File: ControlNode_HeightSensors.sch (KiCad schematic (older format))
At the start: 2 parts

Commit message: Update height sensors.
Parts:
- removed P? (x2): CONN_01X05, symbol CONN_01X05
- added C? (x3): C_100nF_50V, RLOOP_FOOTPRINTS:rLoop_C_0603, symbol C_100nF_50V
- added P? (x3): TE_640456-8, RLOOP_FOOTPRINTS:rLoop_TE640456-8, symbol TE_640456-8
- added R? (x3): 2.2K, RLOOP_FOOTPRINTS:rLoop_R_0603, symbol 2.2K
- added U? (x3): DS8921AMX, RLOOP_FOOTPRINTS:rLoop_SOIC8, symbol DS8921AMX
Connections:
- net labels added: +24V_A, +5V_A, GNDD, HEIGHT_FL_RX_3V, HEIGHT_FL_TX, HEIGHT_FR_RX_3V, HEIGHT_FR_TX, HEIGHT_RL_RX_3V, HEIGHT_RL_TX
- net labels removed: +24V, A2, A3, GND
- wire segments 16 -> 57
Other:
- note removed: "Height Sensors 5 Pin"

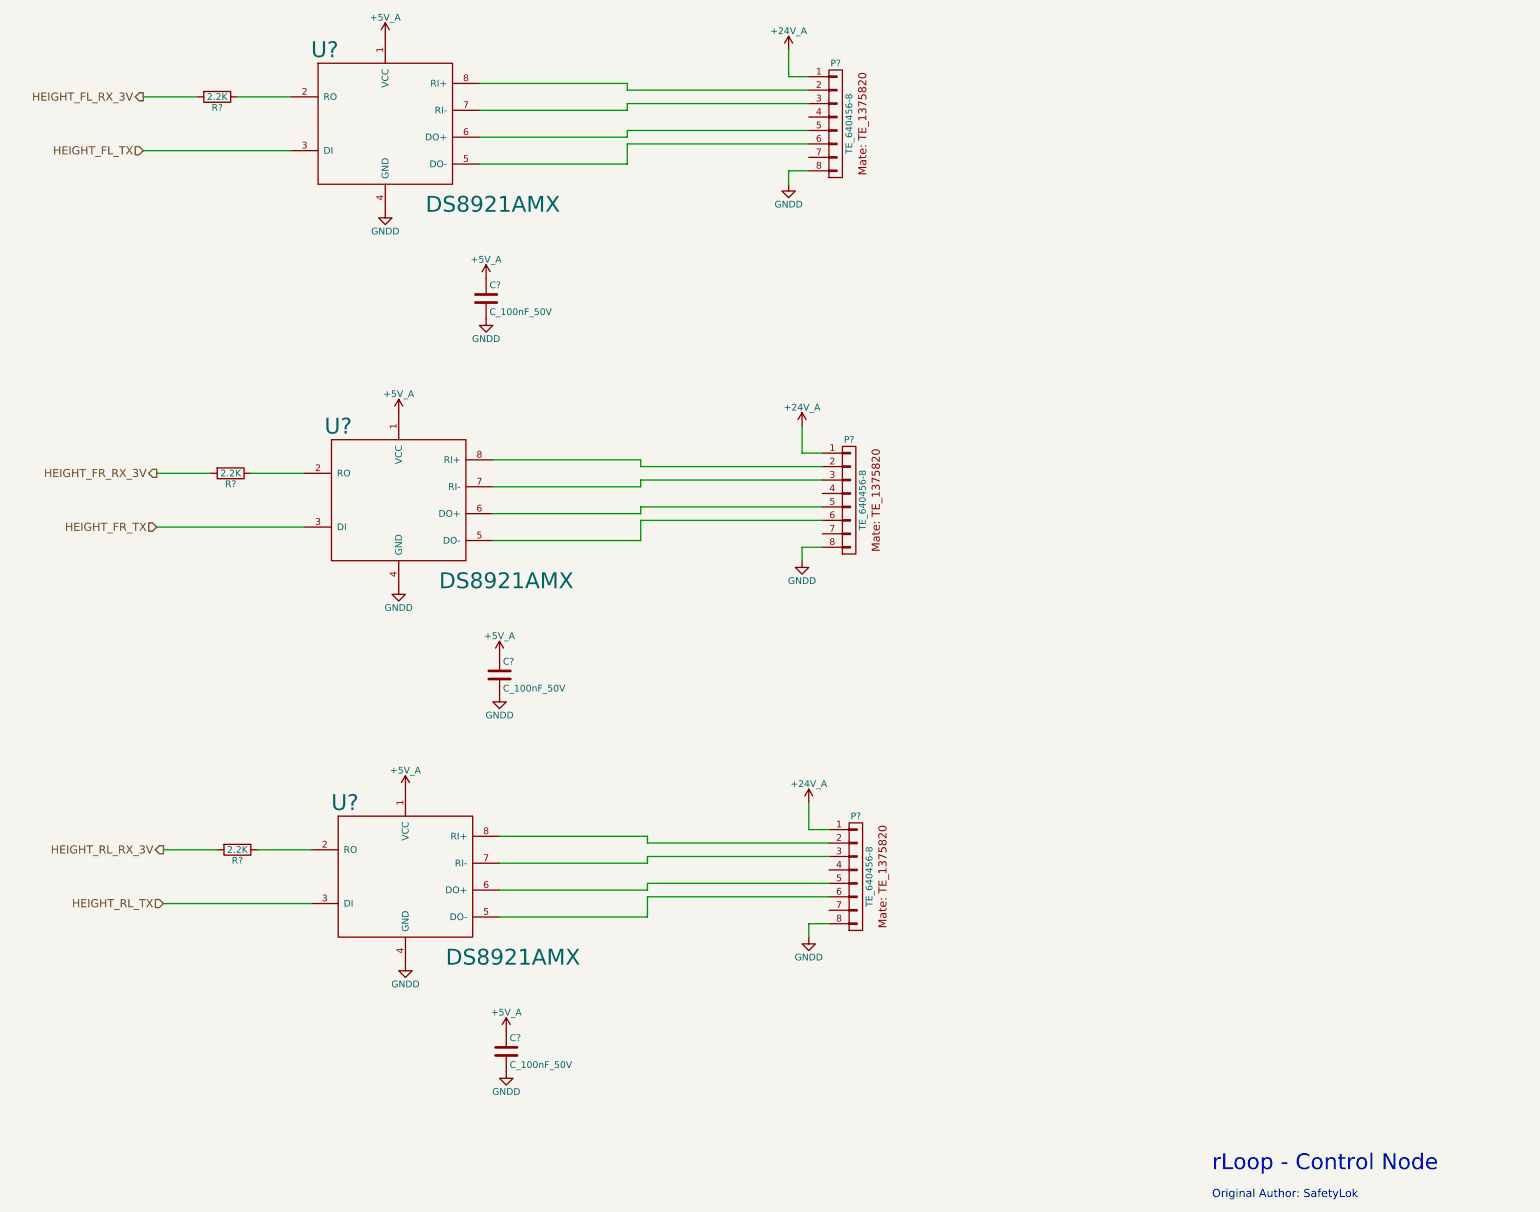
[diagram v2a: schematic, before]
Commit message: Update 10K pullups, 100R on RS422's and additional bypass caps.
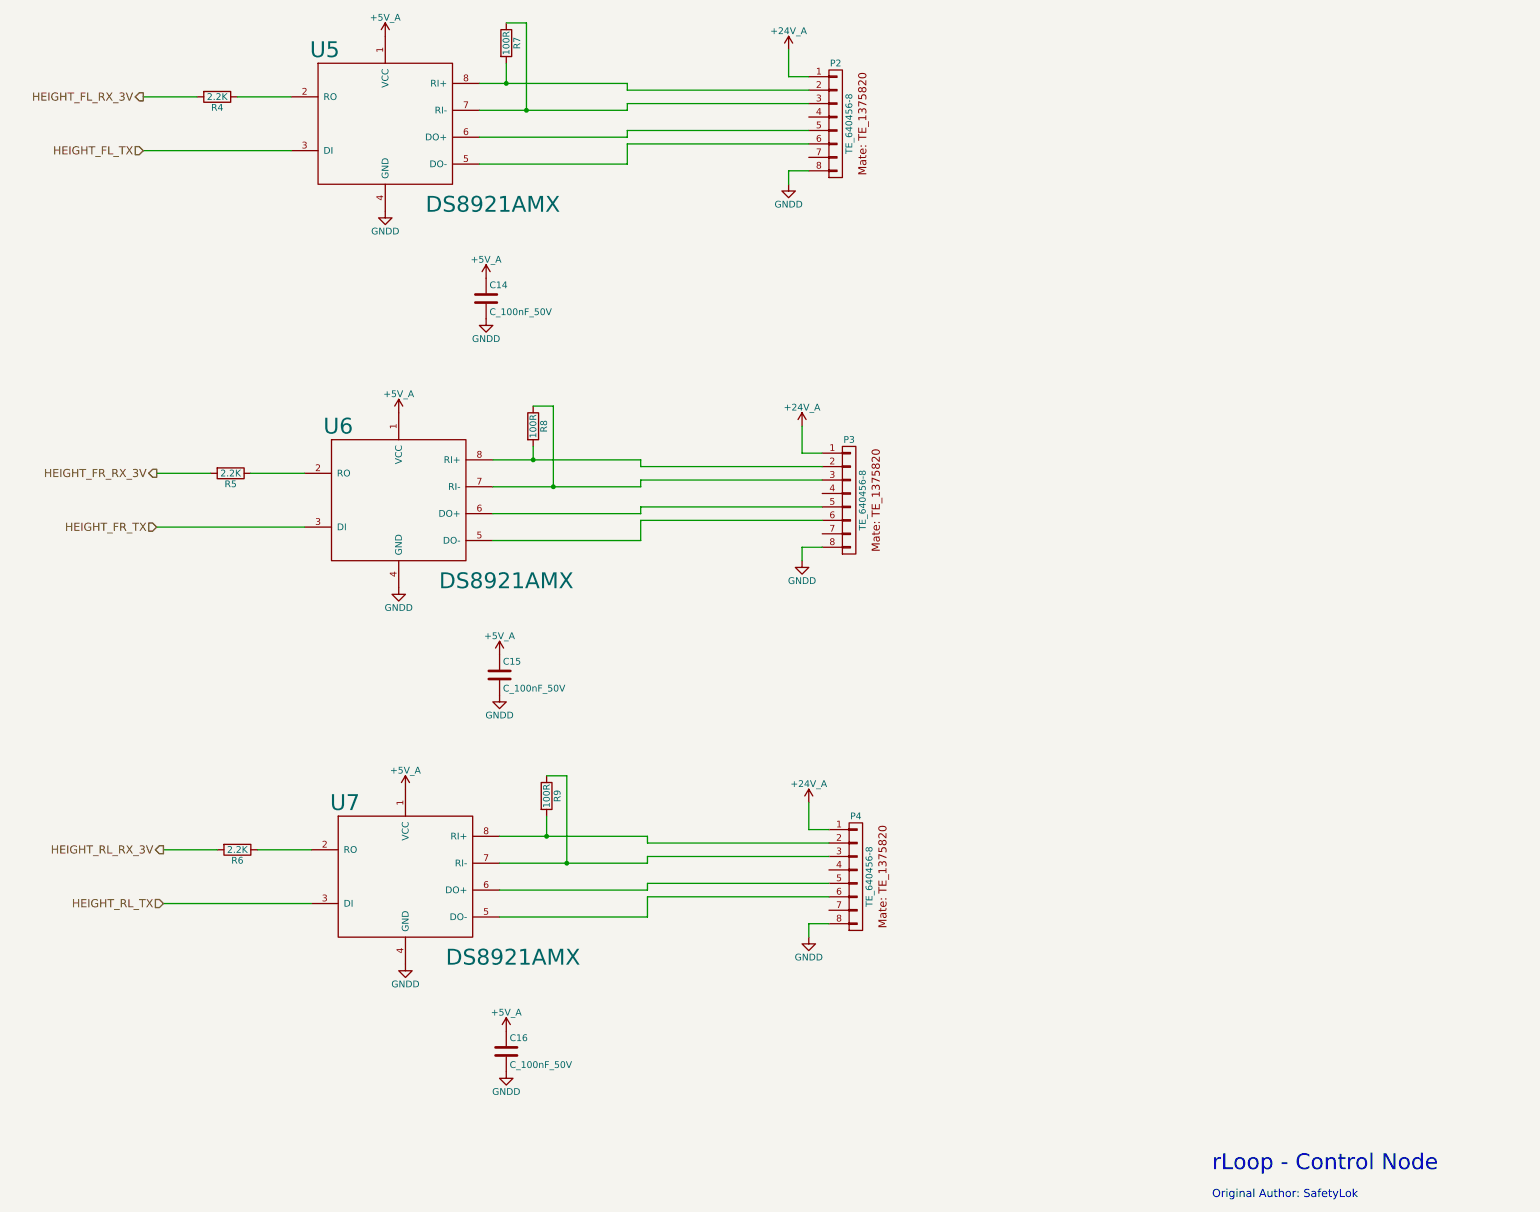
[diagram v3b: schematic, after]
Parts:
- added R7, R8, R9: 100R, RLOOP_FOOTPRINTS:rLoop_R_0603, symbol 100R
- gave numbers to parts that had none: 12
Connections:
- net at P2.2 (P2), U5.8 (RI+): now also R7.2
- net at P2.3 (P3), U5.7 (RI-): now also R7.1
- net at P3.2 (P2), U6.8 (RI+): now also R8.2
- net at P3.3 (P3), U6.7 (RI-): now also R8.1
- net at P4.2 (P2), U7.8 (RI+): now also R9.2
- net at P4.3 (P3), U7.7 (RI-): now also R9.1
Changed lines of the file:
@@
 Original Author: SafetyLok
 $Comp
-L TE_640456-8 P?
+L TE_640456-8 P2
 U 1 1 575BF630
 P 9100 2000
-F 0 "P?" H 9150 2050 50  0000 C CNN
+F 0 "P2" H 9150 2050 50  0000 C CNN
 F 1 "TE_640456-8" V 9250 1600 50  0000 C CNN
 F 2 "RLOOP_FOOTPRINTS:rLoop_TE640456-8" H 9150 1600 50  0001 C CNN
@@
 $EndComp
 $Comp
-L +24V_A #PWR?
+L +24V_A #PWR58
 U 1 1 575BF637
 P 8800 1850
-F 0 "#PWR?" H 8800 1700 50  0001 C CNN
+F 0 "#PWR58" H 8800 1700 50  0001 C CNN
 F 1 "+24V_A" H 8800 1990 50  0000 C CNN
 F 2 "" H 8800 1850 60  0000 C CNN
@@
 $EndComp
 $Comp
-L GNDD #PWR?
+L GNDD #PWR59
 U 1 1 575BF63D
 P 8800 2850
-F 0 "#PWR?" H 8800 2600 50  0001 C CNN
+F 0 "#PWR59" H 8800 2600 50  0001 C CNN
 F 1 "GNDD" H 8800 2700 50  0000 C CNN
 F 2 "" H 8800 2850 50  0000 C CNN
@@
 	8800 2750 8800 2850
 $Comp
-L DS8921AMX U?
+L DS8921AMX U5
 U 1 1 575BF647
 P 5300 1950
-F 0 "U?" H 5350 2050 118 0000 C CNN
+F 0 "U5" H 5350 2050 118 0000 C CNN
 F 1 "DS8921AMX" H 6600 900 118 0000 C CNN
 F 2 "RLOOP_FOOTPRINTS:rLoop_SOIC8" H 5250 1950 118 0001 C CNN
@@
 $EndComp
 $Comp
-L GNDD #PWR?
+L GNDD #PWR47
 U 1 1 575BF64E
 P 5800 3050
-F 0 "#PWR?" H 5800 2800 50  0001 C CNN
+F 0 "#PWR47" H 5800 2800 50  0001 C CNN
 F 1 "GNDD" H 5800 2900 50  0000 C CNN
 F 2 "" H 5800 3050 50  0000 C CNN
@@
 $EndComp
 $Comp
-L C_100nF_50V C?
+L C_100nF_50V C14
 U 1 1 575BF654
 P 6550 3700
-F 0 "C?" H 6575 3800 50  0000 L CNN
+F 0 "C14" H 6575 3800 50  0000 L CNN
 F 1 "C_100nF_50V" H 6575 3600 50  0000 L CNN
 F 2 "RLOOP_FOOTPRINTS:rLoop_C_0603" H 6588 3550 50  0001 C CNN
@@
 $EndComp
 $Comp
-L GNDD #PWR?
+L GNDD #PWR53
 U 1 1 575BF65B
 P 6550 3850
-F 0 "#PWR?" H 6550 3600 50  0001 C CNN
+F 0 "#PWR53" H 6550 3600 50  0001 C CNN
 F 1 "GNDD" H 6550 3700 50  0000 C CNN
 F 2 "" H 6550 3850 50  0000 C CNN
@@
 	7600 2550 8950 2550
 $Comp
-L +5V_A #PWR?
+L +5V_A #PWR46
 U 1 1 575BF66D
 P 5800 1750
-F 0 "#PWR?" H 5800 1600 50  0001 C CNN
+F 0 "#PWR46" H 5800 1600 50  0001 C CNN
 F 1 "+5V_A" H 5800 1890 50  0000 C CNN
 F 2 "" H 5800 1750 60  0000 C CNN
@@
 $EndComp
 $Comp
-L +5V_A #PWR?
+L +5V_A #PWR52
 U 1 1 575BF673
 P 6550 3550
-F 0 "#PWR?" H 6550 3400 50  0001 C CNN
+F 0 "#PWR52" H 6550 3400 50  0001 C CNN
 F 1 "+5V_A" H 6550 3690 50  0000 C CNN
 F 2 "" H 6550 3550 60  0000 C CNN
@@
 $EndComp
 $Comp
-L 2.2K R?
+L 2.2K R4
 U 1 1 575BF679
 P 4550 2200
-F 0 "R?" V 4630 2200 50  0000 C CNN
+F 0 "R4" V 4630 2200 50  0000 C CNN
 F 1 "2.2K" V 4550 2200 50  0000 C CNN
 F 2 "RLOOP_FOOTPRINTS:rLoop_R_0603" V 4480 2200 50  0001 C CNN
@@
 HEIGHT_FL_TX
 $Comp
-L TE_640456-8 P?
+L TE_640456-8 P3
 U 1 1 575BF685
 P 9200 4800
-F 0 "P?" H 9250 4850 50  0000 C CNN
+F 0 "P3" H 9250 4850 50  0000 C CNN
 F 1 "TE_640456-8" V 9350 4400 50  0000 C CNN
 F 2 "RLOOP_FOOTPRINTS:rLoop_TE640456-8" H 9250 4400 50  0001 C CNN
@@
 $EndComp
 $Comp
-L +24V_A #PWR?
+L +24V_A #PWR60
 U 1 1 575BF68C
 P 8900 4650
-F 0 "#PWR?" H 8900 4500 50  0001 C CNN
+F 0 "#PWR60" H 8900 4500 50  0001 C CNN
 F 1 "+24V_A" H 8900 4790 50  0000 C CNN
 F 2 "" H 8900 4650 60  0000 C CNN
@@
 $EndComp
 $Comp
-L GNDD #PWR?
+L GNDD #PWR61
 U 1 1 575BF692
 P 8900 5650
-F 0 "#PWR?" H 8900 5400 50  0001 C CNN
+F 0 "#PWR61" H 8900 5400 50  0001 C CNN
 F 1 "GNDD" H 8900 5500 50  0000 C CNN
 F 2 "" H 8900 5650 50  0000 C CNN
@@
 	8900 5550 8900 5650
 $Comp
-L DS8921AMX U?
+L DS8921AMX U6
 U 1 1 575BF69C
 P 5400 4750
-F 0 "U?" H 5450 4850 118 0000 C CNN
+F 0 "U6" H 5450 4850 118 0000 C CNN
 F 1 "DS8921AMX" H 6700 3700 118 0000 C CNN
 F 2 "RLOOP_FOOTPRINTS:rLoop_SOIC8" H 5350 4750 118 0001 C CNN
@@
 $EndComp
 $Comp
-L GNDD #PWR?
+L GNDD #PWR49
 U 1 1 575BF6A3
 P 5900 5850
-F 0 "#PWR?" H 5900 5600 50  0001 C CNN
+F 0 "#PWR49" H 5900 5600 50  0001 C CNN
 F 1 "GNDD" H 5900 5700 50  0000 C CNN
 F 2 "" H 5900 5850 50  0000 C CNN
@@
 $EndComp
 $Comp
-L C_100nF_50V C?
+L C_100nF_50V C15
 U 1 1 575BF6A9
 P 6650 6500
-F 0 "C?" H 6675 6600 50  0000 L CNN
+F 0 "C15" H 6675 6600 50  0000 L CNN
 F 1 "C_100nF_50V" H 6675 6400 50  0000 L CNN
 F 2 "RLOOP_FOOTPRINTS:rLoop_C_0603" H 6688 6350 50  0001 C CNN
@@
 $EndComp
 $Comp
-L GNDD #PWR?
+L GNDD #PWR55
 U 1 1 575BF6B0
 P 6650 6650
-F 0 "#PWR?" H 6650 6400 50  0001 C CNN
+F 0 "#PWR55" H 6650 6400 50  0001 C CNN
 F 1 "GNDD" H 6650 6500 50  0000 C CNN
 F 2 "" H 6650 6650 50  0000 C CNN
@@
 	7700 5350 9050 5350
 $Comp
-L +5V_A #PWR?
+L +5V_A #PWR48
 U 1 1 575BF6C2
 P 5900 4550
-F 0 "#PWR?" H 5900 4400 50  0001 C CNN
+F 0 "#PWR48" H 5900 4400 50  0001 C CNN
 F 1 "+5V_A" H 5900 4690 50  0000 C CNN
 F 2 "" H 5900 4550 60  0000 C CNN
@@
 $EndComp
 $Comp
-L +5V_A #PWR?
+L +5V_A #PWR54
 U 1 1 575BF6C8
 P 6650 6350
-F 0 "#PWR?" H 6650 6200 50  0001 C CNN
+F 0 "#PWR54" H 6650 6200 50  0001 C CNN
 F 1 "+5V_A" H 6650 6490 50  0000 C CNN
 F 2 "" H 6650 6350 60  0000 C CNN
@@
 $EndComp
 $Comp
-L 2.2K R?
+L 2.2K R5
 U 1 1 575BF6CE
 P 4650 5000
-F 0 "R?" V 4730 5000 50  0000 C CNN
+F 0 "R5" V 4730 5000 50  0000 C CNN
 F 1 "2.2K" V 4650 5000 50  0000 C CNN
 F 2 "RLOOP_FOOTPRINTS:rLoop_R_0603" V 4580 5000 50  0001 C CNN
@@
 HEIGHT_FR_TX
 $Comp
-L TE_640456-8 P?
+L TE_640456-8 P4
 U 1 1 575BF6DA
 P 9250 7600
-F 0 "P?" H 9300 7650 50  0000 C CNN
+F 0 "P4" H 9300 7650 50  0000 C CNN
 F 1 "TE_640456-8" V 9400 7200 50  0000 C CNN
 F 2 "RLOOP_FOOTPRINTS:rLoop_TE640456-8" H 9300 7200 50  0001 C CNN
@@
 $EndComp
 $Comp
-L +24V_A #PWR?
+L +24V_A #PWR62
 U 1 1 575BF6E1
 P 8950 7450
-F 0 "#PWR?" H 8950 7300 50  0001 C CNN
+F 0 "#PWR62" H 8950 7300 50  0001 C CNN
 F 1 "+24V_A" H 8950 7590 50  0000 C CNN
 F 2 "" H 8950 7450 60  0000 C CNN
@@
 $EndComp
 $Comp
-L GNDD #PWR?
+L GNDD #PWR63
 U 1 1 575BF6E7
 P 8950 8450
-F 0 "#PWR?" H 8950 8200 50  0001 C CNN
+F 0 "#PWR63" H 8950 8200 50  0001 C CNN
 F 1 "GNDD" H 8950 8300 50  0000 C CNN
 F 2 "" H 8950 8450 50  0000 C CNN
@@
 	8950 8350 8950 8450
 $Comp
-L DS8921AMX U?
+L DS8921AMX U7
 U 1 1 575BF6F1
 P 5450 7550
-F 0 "U?" H 5500 7650 118 0000 C CNN
+F 0 "U7" H 5500 7650 118 0000 C CNN
 F 1 "DS8921AMX" H 6750 6500 118 0000 C CNN
 F 2 "RLOOP_FOOTPRINTS:rLoop_SOIC8" H 5400 7550 118 0001 C CNN
@@
 $EndComp
 $Comp
-L GNDD #PWR?
+L GNDD #PWR51
 U 1 1 575BF6F8
 P 5950 8650
-F 0 "#PWR?" H 5950 8400 50  0001 C CNN
+F 0 "#PWR51" H 5950 8400 50  0001 C CNN
 F 1 "GNDD" H 5950 8500 50  0000 C CNN
 F 2 "" H 5950 8650 50  0000 C CNN
@@
 $EndComp
 $Comp
-L C_100nF_50V C?
+L C_100nF_50V C16
 U 1 1 575BF6FE
 P 6700 9300
-F 0 "C?" H 6725 9400 50  0000 L CNN
+F 0 "C16" H 6725 9400 50  0000 L CNN
 F 1 "C_100nF_50V" H 6725 9200 50  0000 L CNN
 F 2 "RLOOP_FOOTPRINTS:rLoop_C_0603" H 6738 9150 50  0001 C CNN
@@
 $EndComp
 $Comp
-L GNDD #PWR?
+L GNDD #PWR57
 U 1 1 575BF705
 P 6700 9450
-F 0 "#PWR?" H 6700 9200 50  0001 C CNN
+F 0 "#PWR57" H 6700 9200 50  0001 C CNN
 F 1 "GNDD" H 6700 9300 50  0000 C CNN
 F 2 "" H 6700 9450 50  0000 C CNN
@@
 	7750 8150 9100 8150
 $Comp
-L +5V_A #PWR?
+L +5V_A #PWR50
 U 1 1 575BF717
 P 5950 7350
-F 0 "#PWR?" H 5950 7200 50  0001 C CNN
+F 0 "#PWR50" H 5950 7200 50  0001 C CNN
 F 1 "+5V_A" H 5950 7490 50  0000 C CNN
 F 2 "" H 5950 7350 60  0000 C CNN
@@
 $EndComp
 $Comp
-L +5V_A #PWR?
+L +5V_A #PWR56
 U 1 1 575BF71D
 P 6700 9150
-F 0 "#PWR?" H 6700 9000 50  0001 C CNN
+F 0 "#PWR56" H 6700 9000 50  0001 C CNN
 F 1 "+5V_A" H 6700 9290 50  0000 C CNN
 F 2 "" H 6700 9150 60  0000 C CNN
@@
 $EndComp
 $Comp
-L 2.2K R?
+L 2.2K R6
 U 1 1 575BF723
 P 4700 7800
-F 0 "R?" V 4780 7800 50  0000 C CNN
+F 0 "R6" V 4780 7800 50  0000 C CNN
 F 1 "2.2K" V 4700 7800 50  0000 C CNN
 F 2 "RLOOP_FOOTPRINTS:rLoop_R_0603" V 4630 7800 50  0001 C CNN
@@
 Text HLabel 4150 8200 0    60   Input ~ 0
 HEIGHT_RL_TX
+$Comp
+L 100R R7
+U 1 1 575CB8DE
+P 6700 1800
+F 0 "R7" V 6780 1800 50  0000 C CNN
+F 1 "100R" V 6700 1800 50  0000 C CNN
+F 2 "RLOOP_FOOTPRINTS:rLoop_R_0603" V 6630 1800 50  0001 C CNN
+F 3 "" H 6700 1800 50  0000 C CNN
+	1    6700 1800
+	1    0    0    -1
+$EndComp
+Wire Wire Line
+	6700 1950 6700 2100
+Connection ~ 6700 2100
+Wire Wire Line
+	6700 1650 6850 1650
+Wire Wire Line
+	6850 1650 6850 2300
+Connection ~ 6850 2300
+$Comp
+L 100R R8
+U 1 1 575CBA71
+P 6900 4650
+F 0 "R8" V 6980 4650 50  0000 C CNN
+F 1 "100R" V 6900 4650 50  0000 C CNN
+F 2 "RLOOP_FOOTPRINTS:rLoop_R_0603" V 6830 4650 50  0001 C CNN
+F 3 "" H 6900 4650 50  0000 C CNN
+	1    6900 4650
+	1    0    0    -1
+$EndComp
+Wire Wire Line
+	6900 4800 6900 4900
+Connection ~ 6900 4900
+Wire Wire Line
+	6900 4500 7050 4500
+Wire Wire Line
+	7050 4500 7050 5100
+Connection ~ 7050 5100
+$Comp
+L 100R R9
+U 1 1 575CBB9D
+P 7000 7400
+F 0 "R9" V 7080 7400 50  0000 C CNN
+F 1 "100R" V 7000 7400 50  0000 C CNN
+F 2 "RLOOP_FOOTPRINTS:rLoop_R_0603" V 6930 7400 50  0001 C CNN
+F 3 "" H 7000 7400 50  0000 C CNN
+	1    7000 7400
+	1    0    0    -1
+$EndComp
+Wire Wire Line
+	7000 7550 7000 7700
+Connection ~ 7000 7700
+Wire Wire Line
+	7000 7250 7150 7250
+Wire Wire Line
+	7150 7250 7150 7900
+Connection ~ 7150 7900
 $EndSCHEMATC
